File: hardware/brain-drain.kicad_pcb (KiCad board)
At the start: 4 copper layers, 180 x 110 mm, 311 parts, among them J10 SATA 22-pin, J11 SATA 22-pin, J12 SATA 22-pin, J13 SATA 22-pin, J21 KPJX-4S-S, J3 microSD, J4 RJ45 GbE magjack UDE RB1-125B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, J40 Fan GND/5V/TACH/PWM, J41 OLED GND/VCC/SCL/SDA, J5 USB-C rpiboot, J50 M.2 M-key, J6 nRPIBOOT, J7 UART0 GND/TX/RX, M1 CM5002016, Q1 2N7002, Q20 AO4407A, Q31 P-FET -30V 6A DFN3x3, Q32 P-FET -30V 6A DFN3x3, Q33 P-FET -30V 6A DFN3x3, Q34 P-FET -30V 6A DFN3x3, Q41 P-FET -30V 6A DFN3x3, Q42 P-FET -30V 6A DFN3x3, Q43 P-FET -30V 6A DFN3x3, Q44 P-FET -30V 6A DFN3x3, Q51 2N7002, Q52 2N7002, Q53 2N7002, Q54 2N7002, Q61 2N7002, Q62 2N7002, Q63 2N7002, Q64 2N7002, SW1 DIP x8, SW3 door microswitch, U1 USB5744/2G, U10 ASM1153E, U11 ASM1153E, U12 ASM1153E, U13 ASM1153E, U2 USB5744/2G, U20 TPS56637RPAR, U21 TPS56637RPAR, U22 AP63203WU-7, U3 AP2112K-1.2, U50 TPS22965DSGR, U51 AP63203WU-7, U52 TPS22965DSGR, Y1 25MHz CL=20pF, Y10 30MHz CL=16pF, Y11 30MHz CL=16pF, Y12 30MHz CL=16pF, Y13 30MHz CL=16pF, Y2 25MHz CL=20pF

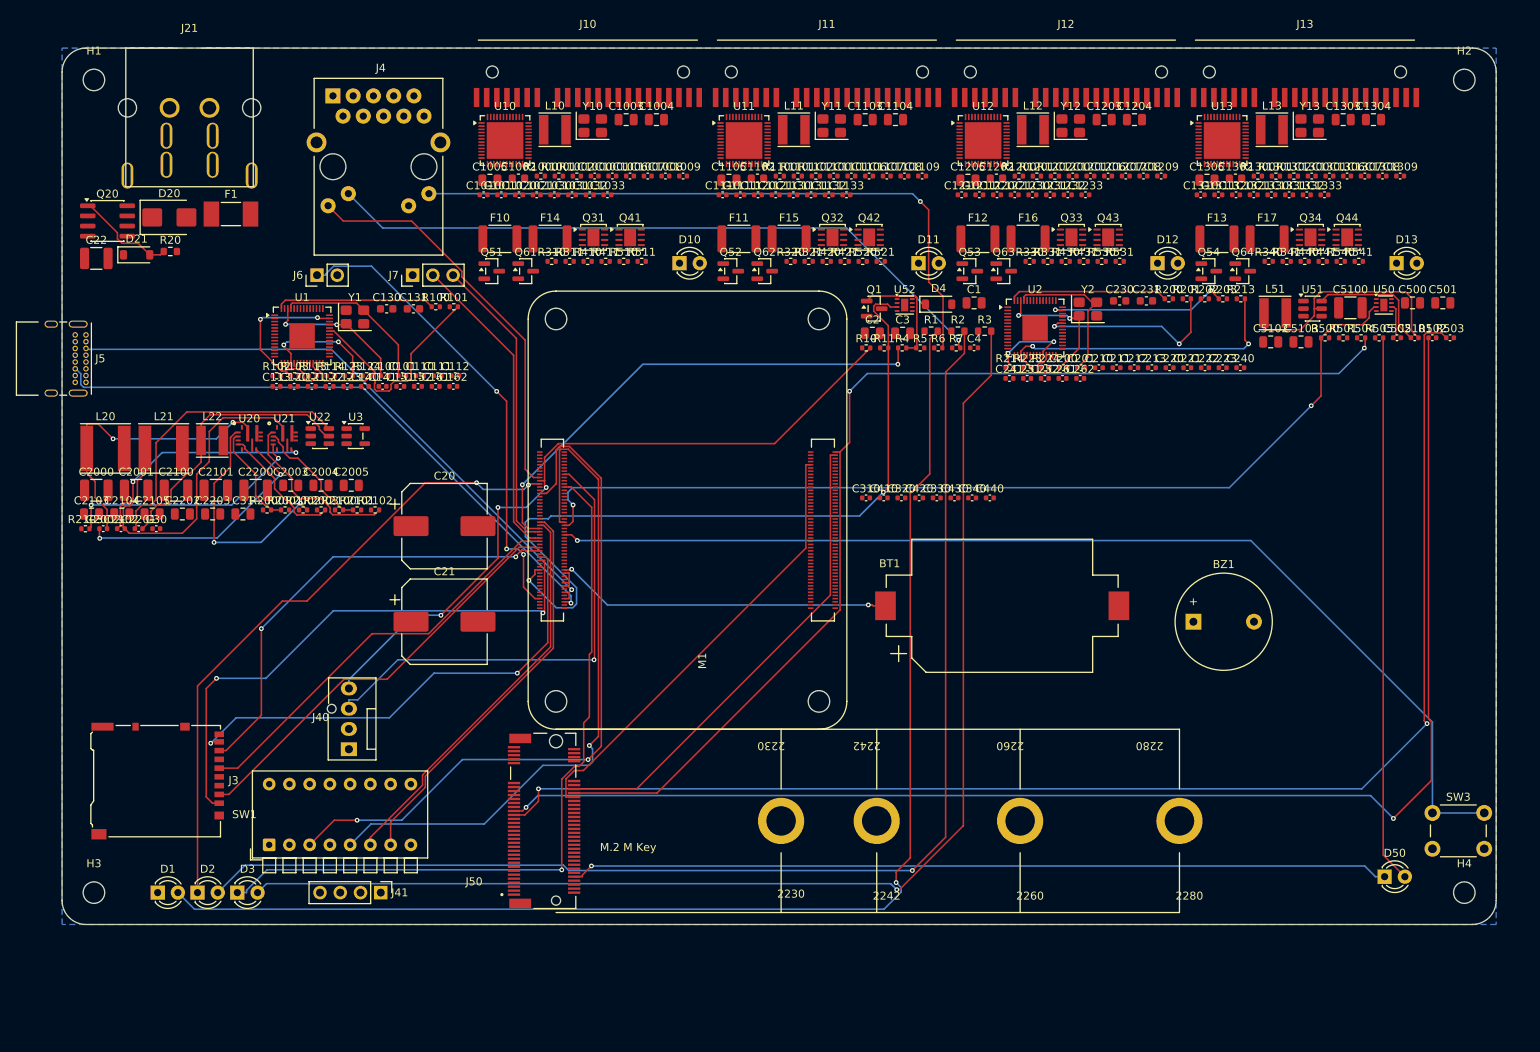
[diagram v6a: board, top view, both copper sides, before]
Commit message: design: portable brain box (C21) — board re-laid out at 150x98, cabled bays, enclosure v1, renders
- gen_pcb.py: new outline, walls (SATA rear; DIN/RJ45/USB-C left; microSD + M.2 slot front),
  CM5 landscape, M.2 vertical along the right edge, CR2032/buzzer on the bottom side
  (pcbnew flip post-process); check_place.py courtyard/outline checker; render_board.sh
- route.py: zones follow the new layout (polygon zones), origin/size from gen_pcb
- enclosure: closed box, drive rack removed, front-wall M.2 slot door, right-wall vents,
  buzzer floor holes, OLED window over the M.2 column; scene with four loose drives on cables;
  stl_preview camera fixed and triangles subdivided
- docs: C21 + D6 (option B parked), decision brief, STATUS R16-R18, panels for three walls,
  README/ARCHITECTURE/USAGE/BOM/CHANGELOG/HISTORY/tracker updated

Co-Authored-By: Claude Fable 5.1 <noreply@anthropic.com>
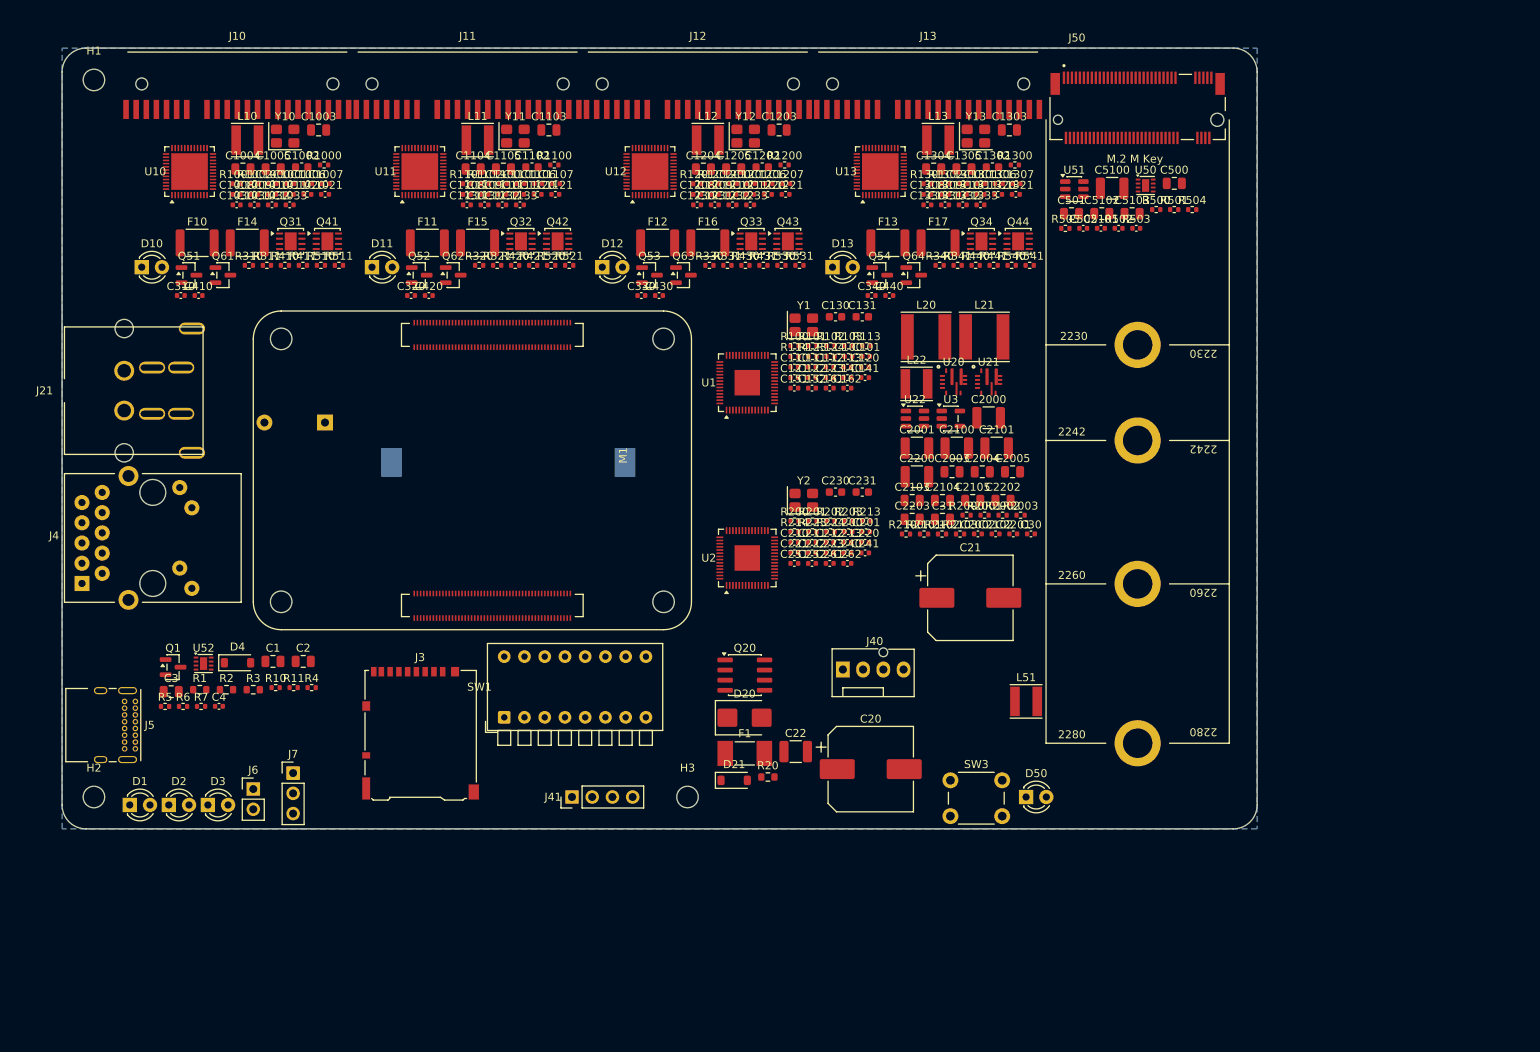
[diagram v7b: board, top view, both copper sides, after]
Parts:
- removed the C440 at (136.4, 76.5)
- BT1, BZ1: moved to B.Cu
- C1: renamed from R3; value 1k -> 22u 10V; footprint Resistor_SMD:R_0603_1608Metric -> Capacitor_SMD:C_0805_2012Metric
- C100: renamed from C112; value 100n -> 33p
- C1000: renamed from C1006; value 100n -> 22p
- C1001: renamed from C1007; value 100n -> 22p
- C1002: renamed from R1001; value 10k -> 2.2u; footprint Resistor_SMD:R_0402_1005Metric -> Capacitor_SMD:C_0603_1608Metric
- C1004: renamed from C1002; value 2.2u -> 10u 10V; footprint Capacitor_SMD:C_0603_1608Metric -> Capacitor_SMD:C_0805_2012Metric
- C1005: renamed from R1000; value 12.1k 1% -> 10u 10V; footprint Resistor_SMD:R_0402_1005Metric -> Capacitor_SMD:C_0805_2012Metric
- C101: renamed from C113; value 100n -> 33p
- C1020: renamed from C1030; value 10n -> 100n
- C1021: renamed from C1031; value 10n -> 100n
- C1032: renamed from F10; value 3A hold 1812 -> 10n; footprint Fuse:Fuse_1812_4532Metric -> Capacitor_SMD:C_0402_1005Metric
- C1033: renamed from F14; value 2A hold 1812 -> 10n; footprint Fuse:Fuse_1812_4532Metric -> Capacitor_SMD:C_0402_1005Metric
- C1101: renamed from C1106; value 100n -> 22p
- C1102: renamed from R1100; value 12.1k 1% -> 2.2u; footprint Resistor_SMD:R_0402_1005Metric -> Capacitor_SMD:C_0603_1608Metric
- C1105: renamed from C1102; value 2.2u -> 10u 10V; footprint Capacitor_SMD:C_0603_1608Metric -> Capacitor_SMD:C_0805_2012Metric
- C1121: renamed from C1130; value 10n -> 100n
- C1133: renamed from F11; value 3A hold 1812 -> 10n; footprint Fuse:Fuse_1812_4532Metric -> Capacitor_SMD:C_0402_1005Metric
- C130: renamed from R102; value 10k -> 4.7u 10V; footprint Resistor_SMD:R_0402_1005Metric -> Capacitor_SMD:C_0603_1608Metric
- C1300: renamed from R1302; value 470 -> 22p; footprint Resistor_SMD:R_0402_1005Metric -> Capacitor_SMD:C_0402_1005Metric
- C1302: renamed from C1305; value 10u 10V -> 2.2u; footprint Capacitor_SMD:C_0805_2012Metric -> Capacitor_SMD:C_0603_1608Metric
- C1303: renamed from Y13; value 30MHz CL=16pF -> 10u 10V; footprint Crystal:Crystal_SMD_3225-4Pin_3.2x2.5mm -> Capacitor_SMD:C_0805_2012Metric
- C1306: renamed from C1301; value 22p -> 100n
- C131: renamed from R103; value 200k -> 4.7u 10V; footprint Resistor_SMD:R_0402_1005Metric -> Capacitor_SMD:C_0603_1608Metric
- C1330: renamed from C1321; value 100n -> 10n
- C151: renamed from U2; value USB5744/2G -> 100n; footprint Package_DFN_QFN:QFN-56-1EP_7x7mm_P0.4mm_EP3.2x3.2mm -> Capacitor_SMD:C_0402_1005Metric
- C152: renamed from Y2; value 25MHz CL=20pF -> 100n; footprint Crystal:Crystal_SMD_3225-4Pin_3.2x2.5mm -> Capacitor_SMD:C_0402_1005Metric
- C161: renamed from C230; value 4.7u 10V -> 100n; footprint Capacitor_SMD:C_0603_1608Metric -> Capacitor_SMD:C_0402_1005Metric
- C162: renamed from C231; value 4.7u 10V -> 100n; footprint Capacitor_SMD:C_0603_1608Metric -> Capacitor_SMD:C_0402_1005Metric
- C2: renamed from R10; value 10k -> 22u 10V; footprint Resistor_SMD:R_0402_1005Metric -> Capacitor_SMD:C_0805_2012Metric
- C20: renamed from J21; value KPJX-4S-S -> 680u 25V low-ESR; footprint brain-drain:Kycon_KPJX-4S-S -> Capacitor_SMD:CP_Elec_10x10.5
- C200: renamed from C211; value 100n -> 33p
- C2000: renamed from C2004; value 22u 10V -> 10u 25V; footprint Capacitor_SMD:C_0805_2012Metric -> Capacitor_SMD:C_1210_3225Metric
- C2001: renamed from C2005; value 22u 10V -> 10u 25V; footprint Capacitor_SMD:C_0805_2012Metric -> Capacitor_SMD:C_1210_3225Metric
- C2002: renamed from C5100; value 10u 25V -> 100n 25V; footprint Capacitor_SMD:C_1210_3225Metric -> Capacitor_SMD:C_0402_1005Metric
- C2005: renamed from C31; value 10u 10V -> 22u 10V
- C201: renamed from C212; value 100n -> 33p
- C2100: renamed from C2103; value 22u 10V -> 10u 25V; footprint Capacitor_SMD:C_0805_2012Metric -> Capacitor_SMD:C_1210_3225Metric
- C2101: renamed from C2104; value 22u 10V -> 10u 25V; footprint Capacitor_SMD:C_0805_2012Metric -> Capacitor_SMD:C_1210_3225Metric
- C2102: renamed from U50; value TPS22965DSGR -> 100n 25V; footprint Package_SON:Texas_DSG0008A_WSON-8-1EP_2x2mm_P0.5mm_EP0.9x1.6mm -> Capacitor_SMD:C_0402_1005Metric
- C2103: renamed from R2000; value 73.2k -> 22u 10V; footprint Resistor_SMD:R_0402_1005Metric -> Capacitor_SMD:C_0805_2012Metric
- C2104: renamed from R2001; value 10k -> 22u 10V; footprint Resistor_SMD:R_0402_1005Metric -> Capacitor_SMD:C_0805_2012Metric
- C2105: renamed from R2002; value 100k -> 22u 10V; footprint Resistor_SMD:R_0402_1005Metric -> Capacitor_SMD:C_0805_2012Metric
- C22: renamed from U20; value TPS56637RPAR -> 10u 25V; footprint brain-drain:Texas_RPA0010A_VQFN-HR-10_3x3mm -> Capacitor_SMD:C_1210_3225Metric
- C2200: renamed from C2105; value 22u 10V -> 10u 25V; footprint Capacitor_SMD:C_0805_2012Metric -> Capacitor_SMD:C_1210_3225Metric
- C2201: renamed from C500; value 10u 10V -> 100n 10V; footprint Capacitor_SMD:C_0805_2012Metric -> Capacitor_SMD:C_0402_1005Metric
- C2202: renamed from R2003; value 10k -> 22u 10V; footprint Resistor_SMD:R_0402_1005Metric -> Capacitor_SMD:C_0805_2012Metric
- C2203: renamed from R2100; value 73.2k -> 22u 10V; footprint Resistor_SMD:R_0402_1005Metric -> Capacitor_SMD:C_0805_2012Metric
- C230: renamed from R201; value 10k -> 4.7u 10V; footprint Resistor_SMD:R_0402_1005Metric -> Capacitor_SMD:C_0603_1608Metric
- C231: renamed from R202; value 10k -> 4.7u 10V; footprint Resistor_SMD:R_0402_1005Metric -> Capacitor_SMD:C_0603_1608Metric
- C252: renamed from U10; value ASM1153E -> 100n; footprint Package_DFN_QFN:QFN-48-1EP_6x6mm_P0.4mm_EP4.6x4.6mm -> Capacitor_SMD:C_0402_1005Metric
- C261: renamed from L10; value 4.7u 1A -> 100n; footprint Inductor_SMD:L_Taiyo-Yuden_NR-40xx -> Capacitor_SMD:C_0402_1005Metric
- C262: renamed from Y10; value 30MHz CL=16pF -> 100n; footprint Crystal:Crystal_SMD_3225-4Pin_3.2x2.5mm -> Capacitor_SMD:C_0402_1005Metric
- C3: renamed from R11; value 10k -> 10u 10V; footprint Resistor_SMD:R_0402_1005Metric -> Capacitor_SMD:C_0805_2012Metric
- C30: renamed from C501; value 22u 10V -> 1u 10V; footprint Capacitor_SMD:C_0805_2012Metric -> Capacitor_SMD:C_0402_1005Metric
- C31: renamed from R2101; value 10k -> 10u 10V; footprint Resistor_SMD:R_0402_1005Metric -> Capacitor_SMD:C_0805_2012Metric
- C310: renamed from U11; value ASM1153E -> 100n; footprint Package_DFN_QFN:QFN-48-1EP_6x6mm_P0.4mm_EP4.6x4.6mm -> Capacitor_SMD:C_0402_1005Metric
- C340: renamed from R541; value 1k -> 100n; footprint Resistor_SMD:R_0402_1005Metric -> Capacitor_SMD:C_0402_1005Metric
- C4: renamed from R100; value 12.0k 1% -> 1u 10V; footprint Resistor_SMD:R_0402_1005Metric -> Capacitor_SMD:C_0402_1005Metric
- C410: renamed from L11; value 4.7u 1A -> 100n; footprint Inductor_SMD:L_Taiyo-Yuden_NR-40xx -> Capacitor_SMD:C_0402_1005Metric
- C420: renamed from U12; value ASM1153E -> 100n; footprint Package_DFN_QFN:QFN-48-1EP_6x6mm_P0.4mm_EP4.6x4.6mm -> Capacitor_SMD:C_0402_1005Metric
- C500: renamed from R501; value 10k -> 10u 10V; footprint Resistor_SMD:R_0402_1005Metric -> Capacitor_SMD:C_0805_2012Metric
- C501: renamed from R504; value 10k -> 22u 10V; footprint Resistor_SMD:R_0402_1005Metric -> Capacitor_SMD:C_0805_2012Metric
- C502: renamed from U52; value TPS22965DSGR -> 1n; footprint Package_SON:Texas_DSG0008A_WSON-8-1EP_2x2mm_P0.5mm_EP0.9x1.6mm -> Capacitor_SMD:C_0402_1005Metric
- C5100: renamed from C5103; value 22u 10V -> 10u 25V; footprint Capacitor_SMD:C_0805_2012Metric -> Capacitor_SMD:C_1210_3225Metric
- C5101: renamed from D4; value 1N4148W -> 100n 10V; footprint Diode_SMD:D_SOD-123 -> Capacitor_SMD:C_0402_1005Metric
- C5102: renamed from R505; value 470 -> 22u 10V; footprint Resistor_SMD:R_0402_1005Metric -> Capacitor_SMD:C_0805_2012Metric
- C5103: renamed from C502; value 1n -> 22u 10V; footprint Capacitor_SMD:C_0402_1005Metric -> Capacitor_SMD:C_0805_2012Metric
- D10: renamed from J12; value SATA 22-pin -> blue bay activity; footprint brain-drain:SATA_22pin_Receptacle_RA -> LED_THT:LED_D3.0mm
- D12: renamed from SW3; value door microswitch -> blue bay activity; footprint Button_Switch_THT:SW_PUSH_6mm -> LED_THT:LED_D3.0mm
- D13: renamed from F1; value 10A slow 0453010.MR -> blue bay activity; footprint Fuse:Fuse_Littelfuse-NANO2-451_453 -> LED_THT:LED_D3.0mm
- D20: renamed from L21; value 2.2u 8A -> SMBJ15A; footprint Inductor_SMD:L_Taiyo-Yuden_NR-60xx -> Diode_SMD:D_SMB
- D21: renamed from U21; value TPS56637RPAR -> 12V 0.5W; footprint brain-drain:Texas_RPA0010A_VQFN-HR-10_3x3mm -> Diode_SMD:D_SOD-123
- D4: renamed from R2; value 1k -> 1N4148W; footprint Resistor_SMD:R_0603_1608Metric -> Diode_SMD:D_SOD-123
- D50: renamed from D21; value 12V 0.5W -> blue M.2 activity; footprint Diode_SMD:D_SOD-123 -> LED_THT:LED_D3.0mm
- F1: renamed from L22; value 4.7u 3A -> 10A slow 0453010.MR; footprint Inductor_SMD:L_Taiyo-Yuden_NR-40xx -> Fuse:Fuse_Littelfuse-NANO2-451_453
- F10: renamed from Q31; value P-FET -30V 6A DFN3x3 -> 3A hold 1812; footprint Package_DFN_QFN:DFN-8-1EP_3x3mm_P0.65mm_EP1.5x2.25mm -> Fuse:Fuse_1812_4532Metric
- F11: renamed from F15; value 2A hold 1812 -> 3A hold 1812
- F13: renamed from C1333; value 10n -> 3A hold 1812; footprint Capacitor_SMD:C_0402_1005Metric -> Fuse:Fuse_1812_4532Metric
- F14: renamed from Q41; value P-FET -30V 6A DFN3x3 -> 2A hold 1812; footprint Package_DFN_QFN:DFN-8-1EP_3x3mm_P0.65mm_EP1.5x2.25mm -> Fuse:Fuse_1812_4532Metric
- F15: renamed from Q32; value P-FET -30V 6A DFN3x3 -> 2A hold 1812; footprint Package_DFN_QFN:DFN-8-1EP_3x3mm_P0.65mm_EP1.5x2.25mm -> Fuse:Fuse_1812_4532Metric
- F17: renamed from F13; value 3A hold 1812 -> 2A hold 1812
- J10: renamed from D11; value blue bay activity -> SATA 22-pin; footprint LED_THT:LED_D3.0mm -> brain-drain:SATA_22pin_Receptacle_RA
- J12: renamed from D50; value blue M.2 activity -> SATA 22-pin; footprint LED_THT:LED_D3.0mm -> brain-drain:SATA_22pin_Receptacle_RA
- J13: renamed from D20; value SMBJ15A -> SATA 22-pin; footprint Diode_SMD:D_SMB -> brain-drain:SATA_22pin_Receptacle_RA
- J21: renamed from H4; value M2.5 -> KPJX-4S-S; footprint MountingHole:MountingHole_2.7mm_M2.5 -> brain-drain:Kycon_KPJX-4S-S
- J50: renamed from C22; value 10u 25V -> M.2 M-key; footprint Capacitor_SMD:C_1210_3225Metric -> brain-drain:M2_Socket3_MKey_CM5IO
- L10: renamed from C1003; value 10u 10V -> 4.7u 1A; footprint Capacitor_SMD:C_0805_2012Metric -> Inductor_SMD:L_Taiyo-Yuden_NR-40xx
- L11: renamed from Y11; value 30MHz CL=16pF -> 4.7u 1A; footprint Crystal:Crystal_SMD_3225-4Pin_3.2x2.5mm -> Inductor_SMD:L_Taiyo-Yuden_NR-40xx
- L13: renamed from U13; value ASM1153E -> 4.7u 1A; footprint Package_DFN_QFN:QFN-48-1EP_6x6mm_P0.4mm_EP4.6x4.6mm -> Inductor_SMD:L_Taiyo-Yuden_NR-40xx
- L20: renamed from U3; value AP2112K-1.2 -> 2.2u 8A; footprint Package_TO_SOT_SMD:SOT-23-5 -> Inductor_SMD:L_Taiyo-Yuden_NR-60xx
- L21: renamed from C2000; value 10u 25V -> 2.2u 8A; footprint Capacitor_SMD:C_1210_3225Metric -> Inductor_SMD:L_Taiyo-Yuden_NR-60xx
- L22: renamed from C2001; value 10u 25V -> 4.7u 3A; footprint Capacitor_SMD:C_1210_3225Metric -> Inductor_SMD:L_Taiyo-Yuden_NR-40xx
- L51: renamed from C21; value 680u 25V low-ESR -> 4.7u 3A; footprint Capacitor_SMD:CP_Elec_10x10.5 -> Inductor_SMD:L_Taiyo-Yuden_NR-40xx
- Q1: renamed from C3; value 10u 10V -> 2N7002; footprint Capacitor_SMD:C_0805_2012Metric -> Package_TO_SOT_SMD:SOT-23
- Q20: renamed from L20; value 2.2u 8A -> AO4407A; footprint Inductor_SMD:L_Taiyo-Yuden_NR-60xx -> Package_SO:SOIC-8_3.9x4.9mm_P1.27mm
- Q31: renamed from Q51; value 2N7002 -> P-FET -30V 6A DFN3x3; footprint Package_TO_SOT_SMD:SOT-23 -> Package_DFN_QFN:DFN-8-1EP_3x3mm_P0.65mm_EP1.5x2.25mm
- Q34: renamed from F17; value 2A hold 1812 -> P-FET -30V 6A DFN3x3; footprint Fuse:Fuse_1812_4532Metric -> Package_DFN_QFN:DFN-8-1EP_3x3mm_P0.65mm_EP1.5x2.25mm
- Q41: renamed from Q61; value 2N7002 -> P-FET -30V 6A DFN3x3; footprint Package_TO_SOT_SMD:SOT-23 -> Package_DFN_QFN:DFN-8-1EP_3x3mm_P0.65mm_EP1.5x2.25mm
- Q42: renamed from Q52; value 2N7002 -> P-FET -30V 6A DFN3x3; footprint Package_TO_SOT_SMD:SOT-23 -> Package_DFN_QFN:DFN-8-1EP_3x3mm_P0.65mm_EP1.5x2.25mm
- Q51: renamed from R310; value 100k -> 2N7002; footprint Resistor_SMD:R_0402_1005Metric -> Package_TO_SOT_SMD:SOT-23
- Q54: renamed from Q44; value P-FET -30V 6A DFN3x3 -> 2N7002; footprint Package_DFN_QFN:DFN-8-1EP_3x3mm_P0.65mm_EP1.5x2.25mm -> Package_TO_SOT_SMD:SOT-23
- Q61: renamed from R311; value 10k -> 2N7002; footprint Resistor_SMD:R_0402_1005Metric -> Package_TO_SOT_SMD:SOT-23
- Q62: renamed from R320; value 100k -> 2N7002; footprint Resistor_SMD:R_0402_1005Metric -> Package_TO_SOT_SMD:SOT-23
- R1: renamed from R4; footprint Resistor_SMD:R_0402_1005Metric -> Resistor_SMD:R_0603_1608Metric
- R10: renamed from R7; value 470 -> 10k
- R100: renamed from R113; value 10k -> 12.0k 1%
- R1000: renamed from R1002; value 470 -> 12.1k 1%
- R1001: renamed from C1000; value 22p -> 10k; footprint Capacitor_SMD:C_0402_1005Metric -> Resistor_SMD:R_0402_1005Metric
- R1002: renamed from C1001; value 22p -> 470; footprint Capacitor_SMD:C_0402_1005Metric -> Resistor_SMD:R_0402_1005Metric
- R103: renamed from R124; value 10k -> 200k
- R11: renamed from C4; value 1u 10V -> 10k; footprint Capacitor_SMD:C_0402_1005Metric -> Resistor_SMD:R_0402_1005Metric
- R1100: renamed from R1101; value 10k -> 12.1k 1%
- R1101: renamed from R1102; value 470 -> 10k
- R1102: renamed from C1100; value 22p -> 470; footprint Capacitor_SMD:C_0402_1005Metric -> Resistor_SMD:R_0402_1005Metric
- R113: renamed from C100; value 33p -> 10k; footprint Capacitor_SMD:C_0402_1005Metric -> Resistor_SMD:R_0402_1005Metric
- R114: renamed from C101; value 33p -> 10k; footprint Capacitor_SMD:C_0402_1005Metric -> Resistor_SMD:R_0402_1005Metric
- R123: renamed from C110; value 100n -> 10k; footprint Capacitor_SMD:C_0402_1005Metric -> Resistor_SMD:R_0402_1005Metric
- R124: renamed from C111; value 100n -> 10k; footprint Capacitor_SMD:C_0402_1005Metric -> Resistor_SMD:R_0402_1005Metric
- R1300: renamed from C1302; value 2.2u -> 12.1k 1%; footprint Capacitor_SMD:C_0603_1608Metric -> Resistor_SMD:R_0402_1005Metric
- R1301: renamed from R1300; value 12.1k 1% -> 10k
- R1302: renamed from R1301; value 10k -> 470
- R2: renamed from R5; value 100k -> 1k; footprint Resistor_SMD:R_0402_1005Metric -> Resistor_SMD:R_0603_1608Metric
- R20: renamed from U22; value AP63203WU-7 -> 100k; footprint Package_TO_SOT_SMD:TSOT-23-6 -> Resistor_SMD:R_0603_1608Metric
- R200: renamed from R203; value 200k -> 12.0k 1%
- R2000: renamed from R2102; value 100k -> 73.2k
- R2002: renamed from C2002; value 100n 25V -> 100k; footprint Capacitor_SMD:C_0402_1005Metric -> Resistor_SMD:R_0402_1005Metric
- R2003: renamed from C2102; value 100n 25V -> 10k; footprint Capacitor_SMD:C_0402_1005Metric -> Resistor_SMD:R_0402_1005Metric
- R203: renamed from R223; value 10k -> 200k
- R2100: renamed from C2201; value 100n 10V -> 73.2k; footprint Capacitor_SMD:C_0402_1005Metric -> Resistor_SMD:R_0402_1005Metric
- R2101: renamed from C30; value 1u 10V -> 10k; footprint Capacitor_SMD:C_0402_1005Metric -> Resistor_SMD:R_0402_1005Metric
- R2102: renamed from L51; value 4.7u 3A -> 100k; footprint Inductor_SMD:L_Taiyo-Yuden_NR-40xx -> Resistor_SMD:R_0402_1005Metric
- R2103: renamed from U51; value AP63203WU-7 -> 10k; footprint Package_TO_SOT_SMD:TSOT-23-6 -> Resistor_SMD:R_0402_1005Metric
- R214: renamed from C200; value 33p -> 10k; footprint Capacitor_SMD:C_0402_1005Metric -> Resistor_SMD:R_0402_1005Metric
- R223: renamed from C201; value 33p -> 10k; footprint Capacitor_SMD:C_0402_1005Metric -> Resistor_SMD:R_0402_1005Metric
- R224: renamed from C210; value 100n -> 10k; footprint Capacitor_SMD:C_0402_1005Metric -> Resistor_SMD:R_0402_1005Metric
- R3: renamed from R6; value 470 -> 1k; footprint Resistor_SMD:R_0402_1005Metric -> Resistor_SMD:R_0603_1608Metric
- R320: renamed from R321; value 10k -> 100k
- R321: renamed from R420; value 100k -> 10k
- R340: renamed from Q64; value 2N7002 -> 100k; footprint Package_TO_SOT_SMD:SOT-23 -> Resistor_SMD:R_0402_1005Metric
- R341: renamed from R340; value 100k -> 10k
- R4: renamed from U1; value USB5744/2G -> 1k; footprint Package_DFN_QFN:QFN-56-1EP_7x7mm_P0.4mm_EP3.2x3.2mm -> Resistor_SMD:R_0402_1005Metric
- R410: renamed from R510; value 10k -> 100k
- R411: renamed from R511; value 1k -> 10k
- R420: renamed from R421; value 10k -> 100k
- R440: renamed from R341; value 10k -> 100k
- R441: renamed from R440; value 100k -> 10k
- R5: renamed from Y1; value 25MHz CL=20pF -> 100k; footprint Crystal:Crystal_SMD_3225-4Pin_3.2x2.5mm -> Resistor_SMD:R_0402_1005Metric
- R500: renamed from C5101; value 100n 10V -> 10k; footprint Capacitor_SMD:C_0402_1005Metric -> Resistor_SMD:R_0402_1005Metric
- R501: renamed from R502; value 0R (cap DNP alt) -> 10k; footprint Capacitor_SMD:C_0402_1005Metric -> Resistor_SMD:R_0402_1005Metric
- R502: renamed from C1; value 22u 10V -> 0R (cap DNP alt); footprint Capacitor_SMD:C_0805_2012Metric -> Capacitor_SMD:C_0402_1005Metric
- R503: renamed from C2; value 22u 10V -> 0R (cap DNP alt); footprint Capacitor_SMD:C_0805_2012Metric -> Capacitor_SMD:C_0402_1005Metric
- R504: renamed from R503; value 0R (cap DNP alt) -> 10k; footprint Capacitor_SMD:C_0402_1005Metric -> Resistor_SMD:R_0402_1005Metric
- R505: renamed from Q1; value 2N7002 -> 470; footprint Package_TO_SOT_SMD:SOT-23 -> Resistor_SMD:R_0402_1005Metric
- R510: renamed from C310; value 100n -> 10k; footprint Capacitor_SMD:C_0402_1005Metric -> Resistor_SMD:R_0402_1005Metric
- R511: renamed from C410; value 100n -> 1k; footprint Capacitor_SMD:C_0402_1005Metric -> Resistor_SMD:R_0402_1005Metric
- R520: renamed from R521; value 1k -> 10k
- R521: renamed from C320; value 100n -> 1k; footprint Capacitor_SMD:C_0402_1005Metric -> Resistor_SMD:R_0402_1005Metric
- R541: renamed from R540; value 10k -> 1k
- R6: renamed from C130; value 4.7u 10V -> 470; footprint Capacitor_SMD:C_0603_1608Metric -> Resistor_SMD:R_0402_1005Metric
- R7: renamed from C131; value 4.7u 10V -> 470; footprint Capacitor_SMD:C_0603_1608Metric -> Resistor_SMD:R_0402_1005Metric
- SW3: renamed from R20; value 100k -> door microswitch; footprint Resistor_SMD:R_0603_1608Metric -> Button_Switch_THT:SW_PUSH_6mm
- U1: renamed from J10; value SATA 22-pin -> USB5744/2G; footprint brain-drain:SATA_22pin_Receptacle_RA -> Package_DFN_QFN:QFN-56-1EP_7x7mm_P0.4mm_EP3.2x3.2mm
- U10: renamed from J11; value SATA 22-pin -> ASM1153E; footprint brain-drain:SATA_22pin_Receptacle_RA -> Package_DFN_QFN:QFN-48-1EP_6x6mm_P0.4mm_EP4.6x4.6mm
- U11: renamed from D12; value blue bay activity -> ASM1153E; footprint LED_THT:LED_D3.0mm -> Package_DFN_QFN:QFN-48-1EP_6x6mm_P0.4mm_EP4.6x4.6mm
- U12: renamed from J50; value M.2 M-key -> ASM1153E; footprint brain-drain:M2_Socket3_MKey_CM5IO -> Package_DFN_QFN:QFN-48-1EP_6x6mm_P0.4mm_EP4.6x4.6mm
- U13: renamed from Q20; value AO4407A -> ASM1153E; footprint Package_SO:SOIC-8_3.9x4.9mm_P1.27mm -> Package_DFN_QFN:QFN-48-1EP_6x6mm_P0.4mm_EP4.6x4.6mm
- U2: renamed from D10; value blue bay activity -> USB5744/2G; footprint LED_THT:LED_D3.0mm -> Package_DFN_QFN:QFN-56-1EP_7x7mm_P0.4mm_EP3.2x3.2mm
- U20: renamed from C2100; value 10u 25V -> TPS56637RPAR; footprint Capacitor_SMD:C_1210_3225Metric -> brain-drain:Texas_RPA0010A_VQFN-HR-10_3x3mm
- U21: renamed from C2101; value 10u 25V -> TPS56637RPAR; footprint Capacitor_SMD:C_1210_3225Metric -> brain-drain:Texas_RPA0010A_VQFN-HR-10_3x3mm
- U22: renamed from C2200; value 10u 25V -> AP63203WU-7; footprint Capacitor_SMD:C_1210_3225Metric -> Package_TO_SOT_SMD:TSOT-23-6
- U3: renamed from C2003; value 22u 10V -> AP2112K-1.2; footprint Capacitor_SMD:C_0805_2012Metric -> Package_TO_SOT_SMD:SOT-23-5
- U50: renamed from R500; value 10k -> TPS22965DSGR; footprint Resistor_SMD:R_0402_1005Metric -> Package_SON:Texas_DSG0008A_WSON-8-1EP_2x2mm_P0.5mm_EP0.9x1.6mm
- U51: renamed from C5102; value 22u 10V -> AP63203WU-7; footprint Capacitor_SMD:C_0805_2012Metric -> Package_TO_SOT_SMD:TSOT-23-6
- U52: renamed from R1; value 1k -> TPS22965DSGR; footprint Resistor_SMD:R_0603_1608Metric -> Package_SON:Texas_DSG0008A_WSON-8-1EP_2x2mm_P0.5mm_EP0.9x1.6mm
- Y1: renamed from R101; value 10k -> 25MHz CL=20pF; footprint Resistor_SMD:R_0402_1005Metric -> Crystal:Crystal_SMD_3225-4Pin_3.2x2.5mm
- Y10: renamed from C1004; value 10u 10V -> 30MHz CL=16pF; footprint Capacitor_SMD:C_0805_2012Metric -> Crystal:Crystal_SMD_3225-4Pin_3.2x2.5mm
- Y11: renamed from C1103; value 10u 10V -> 30MHz CL=16pF; footprint Capacitor_SMD:C_0805_2012Metric -> Crystal:Crystal_SMD_3225-4Pin_3.2x2.5mm
- Y13: renamed from L13; value 4.7u 1A -> 30MHz CL=16pF; footprint Inductor_SMD:L_Taiyo-Yuden_NR-40xx -> Crystal:Crystal_SMD_3225-4Pin_3.2x2.5mm
- Y2: renamed from R200; value 12.0k 1% -> 25MHz CL=20pF; footprint Resistor_SMD:R_0402_1005Metric -> Crystal:Crystal_SMD_3225-4Pin_3.2x2.5mm
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- renumbered C1005 to C1003, C1008 to C1006, C1009 to C1007, C1010 to C1008, C1011 to C1009, C1020 to C1010, C1021 to C1011, C1032 to C1030, C1033 to C1031, C120 to C110, C1101 to C1100, C1104 to C1103, C1105 to C1104, C1107 to C1106, C1108 to C1107, C1109 to C1108, C1110 to C1109, C121 to C111, C1111 to C1110, C1120 to C1111, C122 to C112, C1121 to C1120, C123 to C113, C1131 to C1130, C1132 to C1131, C1133 to C1132, C140 to C120, C141 to C121, C151 to C122, C152 to C123, C1300 to C1301, C1303 to C1304, C1304 to C1305, C1306 to C1307, C1307 to C1308, C1308 to C1309, C1309 to C1310, C1310 to C1311, C1311 to C1320, C1320 to C1321, C1330 to C1331, C1331 to C1332, C1332 to C1333, C161 to C140, C162 to C141, C2202 to C2003, C2203 to C2004, C20 to C21, C213 to C210, C220 to C211, C221 to C212, C222 to C213, C223 to C220, C240 to C221, C241 to C222, C251 to C223, C252 to C240, C261 to C241, C262 to C251, C420 to C320, C340 to C440, D13 to D11, J13 to J11, Q42 to Q32, Q34 to Q44, Q62 to Q52, Q54 to Q64, R114 to R101, R123 to R102, R2103 to R2001, R213 to R201, R214 to R202, R224 to R213, R410 to R310, R411 to R311, R520 to R421, R441 to R540
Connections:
- C1 pad 1: +3V3 -> 5V_SYS
- C1 pad 2: D3_A -> GND
- C100 pad 1: +3V3 -> U1_XTALI
- C1000 pad 1: U10_VDD_CORE -> U10_XI
- C1001 pad 1: U10_VDD_CORE -> U10_XO
- C1002 pad 1: U10_VCCO -> U10_RST
- C1002 pad 2: U10_RST -> GND
- C1003 pad 1: U10_VCCO -> U10_VDD_CORE
- C1004 pad 1: U10_RST -> 5V_SYS
- C1005 pad 1: U10_REXT -> U10_VCCO
- C1006 pad 1: U10_VCCO -> U10_VDD_CORE
- C1007 pad 1: U10_VCCO -> U10_VDD_CORE
- C101 pad 1: +3V3 -> U1_XTALO
- C1010 pad 1: U10_UTXP -> U10_VCCO
- C1010 pad 2: BAY1_USB3_TX_P -> GND
- C1011 pad 1: U10_UTXN -> U10_VCCO
- C1011 pad 2: BAY1_USB3_TX_N -> GND
- C1020 pad 1: U10_STXP -> U10_UTXP
- C1020 pad 2: BAY1_SATA_A_P -> BAY1_USB3_TX_P
- C1021 pad 1: U10_STXN -> U10_UTXN
- C1021 pad 2: BAY1_SATA_A_N -> BAY1_USB3_TX_N
- C1030 pad 1: BAY1_SATA_B_P -> U10_STXP
- C1030 pad 2: U10_SRXP -> BAY1_SATA_A_P
- C1031 pad 1: BAY1_SATA_B_N -> U10_STXN
- C1031 pad 2: U10_SRXN -> BAY1_SATA_A_N
- C1032 pad 1: 12V_BAY1_SW -> BAY1_SATA_B_P
- C1032 pad 2: 12V_BAY1 -> U10_SRXP
- C1033 pad 1: 5V_BAY1_SW -> BAY1_SATA_B_N
- C1033 pad 2: 5V_BAY1 -> U10_SRXN
- C110 pad 1: +1V2 -> +3V3
- C1100 pad 1: U11_XO -> U11_XI
- C1101 pad 1: U11_VDD_CORE -> U11_XO
- C1102 pad 1: U11_REXT -> U11_RST
- C1103 pad 1: 5V_SYS -> U11_VDD_CORE
- C1104 pad 1: U11_VCCO -> 5V_SYS
- C1105 pad 1: U11_RST -> U11_VCCO
- C1107 pad 1: U11_VCCO -> U11_VDD_CORE
- C111 pad 1: +1V2 -> +3V3
- C1111 pad 1: U11_UTXP -> U11_VCCO
- C1111 pad 2: BAY2_USB3_TX_P -> GND
- C112 pad 1: +1V2 -> +3V3
- C1120 pad 1: U11_UTXN -> U11_UTXP
- C1120 pad 2: BAY2_USB3_TX_N -> BAY2_USB3_TX_P
- C1121 pad 1: U11_STXP -> U11_UTXN
- C1121 pad 2: BAY2_SATA_A_P -> BAY2_USB3_TX_N
- C113 pad 1: +1V2 -> +3V3
- C1130 pad 1: U11_STXN -> U11_STXP
- C1130 pad 2: BAY2_SATA_A_N -> BAY2_SATA_A_P
- C1131 pad 1: BAY2_SATA_B_P -> U11_STXN
- C1131 pad 2: U11_SRXP -> BAY2_SATA_A_N
- C1132 pad 1: BAY2_SATA_B_N -> BAY2_SATA_B_P
- C1132 pad 2: U11_SRXN -> U11_SRXP
- C1133 pad 1: 12V_BAY2_SW -> BAY2_SATA_B_N
- C1133 pad 2: 12V_BAY2 -> U11_SRXN
- C120 pad 1: U1_UP_TXDP -> +1V2
- C120 pad 2: USB3_0_RX_P -> GND
- C121 pad 1: U1_UP_TXDM -> +1V2
- C121 pad 2: USB3_0_RX_N -> GND
- C122 pad 1: U1_DN1_TXDP -> +1V2
- C122 pad 2: BAY1_USB3_RX_P -> GND
- C123 pad 1: U1_DN2_TXDP -> +1V2
- C123 pad 2: BAY2_USB3_RX_P -> GND
- C130 pad 2: U1_RESET_N -> GND
- C1300 pad 1: U13_VCCO -> U13_XI
- C1300 pad 2: BAY4_LED_A -> GND
- C1301 pad 1: U13_XI -> U13_XO
- C1302 pad 1: U13_VCCO -> U13_RST
- C1303 pad 1: U13_XI -> U13_VDD_CORE
- C1304 pad 1: U13_VDD_CORE -> 5V_SYS
- C1305 pad 1: 5V_SYS -> U13_VCCO
- C1306 pad 1: U13_XO -> U13_VDD_CORE
- C1308 pad 1: U13_VDD_CORE -> U13_VCCO
- C131 pad 1: U1_CFG_NON_REM -> +1V2
- C1320 pad 1: U13_VCCO -> U13_UTXP
- C1320 pad 2: GND -> BAY4_USB3_TX_P
- C1321 pad 1: U13_UTXP -> U13_UTXN
- C1321 pad 2: BAY4_USB3_TX_P -> BAY4_USB3_TX_N
- C1330 pad 1: U13_UTXN -> U13_STXP
- C1330 pad 2: BAY4_USB3_TX_N -> BAY4_SATA_A_P
- C1331 pad 1: U13_STXP -> U13_STXN
- C1331 pad 2: BAY4_SATA_A_P -> BAY4_SATA_A_N
- C1332 pad 1: U13_STXN -> BAY4_SATA_B_P
- C1332 pad 2: BAY4_SATA_A_N -> U13_SRXP
- C1333 pad 1: BAY4_SATA_B_P -> BAY4_SATA_B_N
- C1333 pad 2: U13_SRXP -> U13_SRXN
- C140 pad 1: U1_DN1_TXDM -> U1_UP_TXDP
- C140 pad 2: BAY1_USB3_RX_N -> USB3_0_RX_P
- C141 pad 1: U1_DN2_TXDM -> U1_UP_TXDM
- C141 pad 2: BAY2_USB3_RX_N -> USB3_0_RX_N
- C151 pad 1: BAY3_USB2_DP -> U1_DN1_TXDP
- C151 pad 2: BAY3_USB2_DM -> BAY1_USB3_RX_P
- C152 pad 1: U2_XTALI -> U1_DN2_TXDP
- C152 pad 2: GND -> BAY2_USB3_RX_P
- C161 pad 1: +3V3 -> U1_DN1_TXDM
- C161 pad 2: GND -> BAY1_USB3_RX_N
- C162 pad 1: +1V2 -> U1_DN2_TXDM
- C162 pad 2: GND -> BAY2_USB3_RX_N
- C2 pad 1: +3V3 -> 5V_SYS
- C2 pad 2: FAN_PWM -> GND
- C20 pad 1: VIN_12V_RAW -> +12V
- C20 pad 2: VIN_12V_RAW -> GND
- C200 pad 1: +3V3 -> U2_XTALI
- C2000 pad 1: 5V_SYS -> +12V
- C2001 pad 1: 5V_SYS -> +12V
- C2002 pad 1: +12V -> U20_BOOT
- C2002 pad 2: GND -> U20_SW
- C2003 pad 1: +3V3 -> 5V_SYS
- C2004 pad 1: +3V3 -> 5V_SYS
- C2005 pad 1: +1V2 -> 5V_SYS
- C201 pad 1: +3V3 -> U2_XTALO
- C2100 pad 1: 5V_HDD -> +12V
- C2101 pad 1: 5V_HDD -> +12V
- C2102 pad 1: 3V3_M2 -> U21_BOOT
- C2102 pad 2: 3V3_M2 -> U21_SW
- C2103 pad 1: 5V_SYS -> 5V_HDD
- C2103 pad 2: U20_FB -> GND
- C2104 pad 1: U20_FB -> 5V_HDD
- C2105 pad 1: +12V -> 5V_HDD
- C2105 pad 2: U20_EN -> GND
- C211 pad 1: +1V2 -> +3V3
- C212 pad 1: +1V2 -> +3V3
- C213 pad 1: +1V2 -> +3V3
- C22 pad 1: U20_EN -> +12V
- C22 pad 2: U20_FB -> GND
- C2200 pad 1: 5V_HDD -> +12V
- C2201 pad 1: 3V3_M2 -> U22_BST
- C2201 pad 2: GND -> U22_SW
- C2202 pad 1: 5V_SYS -> +3V3
- C2202 pad 2: PG_5V_SYS -> GND
- C2203 pad 1: 5V_HDD -> +3V3
- C2203 pad 2: U21_FB -> GND
- C221 pad 1: U2_UP_TXDP -> +1V2
- C221 pad 2: USB3_1_RX_P -> GND
- C222 pad 1: U2_UP_TXDM -> +1V2
- C222 pad 2: USB3_1_RX_N -> GND
- C223 pad 1: U2_DN1_TXDP -> +1V2
- C223 pad 2: BAY3_USB3_RX_P -> GND
- C230 pad 2: U2_VBUS_DET -> GND
- C231 pad 1: +3V3 -> +1V2
- C231 pad 2: U2_RESET_N -> GND
- C240 pad 1: U2_DN2_TXDP -> U2_UP_TXDP
- C240 pad 2: BAY4_USB3_RX_P -> USB3_1_RX_P
- C241 pad 1: U2_DN1_TXDM -> U2_UP_TXDM
- C241 pad 2: BAY3_USB3_RX_N -> USB3_1_RX_N
- C251 pad 1: U2_DN2_TXDM -> U2_DN1_TXDP
- C251 pad 2: BAY4_USB3_RX_N -> BAY3_USB3_RX_P
- C252 pad 1: 5V_SYS -> U2_DN2_TXDP
- C252 pad 2: (no net) -> BAY4_USB3_RX_P
- C261 pad 1: U10_LXI -> U2_DN1_TXDM
- C261 pad 2: U10_VDD_CORE -> BAY3_USB3_RX_N
- C262 pad 1: U10_XI -> U2_DN2_TXDM
- C262 pad 2: GND -> BAY4_USB3_RX_N
- C3 pad 1: +3V3 -> SD_VDD
- C3 pad 2: SD_PWR_ON -> GND
- C30 pad 1: 3V3_M2_SW -> +3V3
- C31 pad 1: U21_FB -> +1V2
- C310 pad 1: 5V_SYS -> +12V
- C310 pad 2: (no net) -> Q31_G
- C320 pad 1: 5V_HDD -> +12V
- C320 pad 2: Q42_G -> Q32_G
- C340 pad 1: BAY_EN4 -> +12V
- C340 pad 2: BAY4_EN_G -> Q34_G
- C4 pad 1: U1_RBIAS -> +3V3
- C410 pad 1: U11_LXI -> 5V_HDD
- C410 pad 2: U11_VDD_CORE -> Q41_G
- C420 pad 1: 5V_SYS -> 5V_HDD
- C420 pad 2: (no net) -> Q42_G
- C440 pad 1: +12V -> 5V_HDD
- C440 pad 2: Q34_G -> Q44_G
- C500 pad 1: 3V3_M2_SW -> 3V3_M2
- C500 pad 2: M2_PEDET -> GND
- C501 pad 2: PCIE_CLKREQ -> GND
- C502 pad 1: +3V3 -> U50_CT
- C502 pad 2: +3V3 -> GND
- C5100 pad 1: 3V3_M2 -> +12V
- C5101 pad 1: 5V_SYS -> U51_BST
- C5101 pad 2: BZ1_N -> U51_SW
- C5102 pad 1: 3V3_M2_SW -> 3V3_M2
- C5102 pad 2: M2_LED_A -> GND
- C5103 pad 1: U50_CT -> 3V3_M2
- D11 pad 1: U13_LED -> U11_LED
- D11 pad 2: BAY4_LED_A -> BAY2_LED_A
- D12 pad 1: M2_DOOR -> U12_LED
- D12 pad 2: GND -> BAY3_LED_A
- D13 pad 1: VIN_12V_RAW -> U13_LED
- D13 pad 2: VIN_12V_FUSED -> BAY4_LED_A
- D20 pad 1: U21_SW -> GND
- D20 pad 2: 5V_HDD -> VIN_12V_FUSED
- D21 pad 1: U21_EN -> +12V
- D21 pad 2: U21_FB -> Q20_GATE
- D4 pad 1: +3V3 -> 5V_SYS
- D4 pad 2: D2_A -> BZ1_N
- D50 pad 1: +12V -> M2_DAS
- D50 pad 2: Q20_GATE -> M2_LED_A
- F1 pad 1: U22_SW -> VIN_12V_RAW
- F1 pad 2: +3V3 -> VIN_12V_FUSED
- F10 pad 1: Q31_G -> 12V_BAY1_SW
- F10 pad 2: +12V -> 12V_BAY1
- F11 pad 1: 5V_BAY2_SW -> 12V_BAY2_SW
- F11 pad 2: 5V_BAY2 -> 12V_BAY2
- F13 pad 1: BAY4_SATA_B_N -> 12V_BAY4_SW
- F13 pad 2: U13_SRXN -> 12V_BAY4
- F14 pad 1: Q41_G -> 5V_BAY1_SW
- F14 pad 2: 5V_HDD -> 5V_BAY1
- F15 pad 1: Q32_G -> 5V_BAY2_SW
- F15 pad 2: +12V -> 5V_BAY2
- F17 pad 1: 12V_BAY4_SW -> 5V_BAY4_SW
- F17 pad 2: 12V_BAY4 -> 5V_BAY4
- J11 pad P13: 12V_BAY4 -> 12V_BAY2
- J11 pad P14: 12V_BAY4 -> 12V_BAY2
- J11 pad P15: 12V_BAY4 -> 12V_BAY2
- J11 pad P7: 5V_BAY4 -> 5V_BAY2
- J11 pad P8: 5V_BAY4 -> 5V_BAY2
- J11 pad P9: 5V_BAY4 -> 5V_BAY2
- J11 pad S2: BAY4_SATA_A_P -> BAY2_SATA_A_P
- J11 pad S3: BAY4_SATA_A_N -> BAY2_SATA_A_N
- J11 pad S5: BAY4_SATA_B_N -> BAY2_SATA_B_N
- J11 pad S6: BAY4_SATA_B_P -> BAY2_SATA_B_P
- J50 pad 1: +12V -> (no net)
- J50 pad 2: GND -> 3V3_M2_SW
- L10 pad 1: U10_VDD_CORE -> U10_LXI
- L10 pad 2: GND -> U10_VDD_CORE
- L11 pad 1: U11_XI -> U11_LXI
- L11 pad 2: GND -> U11_VDD_CORE
- L13 pad 1: 5V_SYS -> U13_LXI
- L13 pad 2: (no net) -> U13_VDD_CORE
- L20 pad 1: +3V3 -> U20_SW
- L20 pad 2: GND -> 5V_SYS
- L21 pad 1: +12V -> U21_SW
- L21 pad 2: GND -> 5V_HDD
- L22 pad 1: +12V -> U22_SW
- L22 pad 2: GND -> +3V3
- L51 pad 1: +12V -> U51_SW
- L51 pad 2: GND -> 3V3_M2
- Q1 pad 1: SD_VDD -> Q1_GATE
- Q20 pad 1: U20_SW -> Q20_GATE
- Q20 pad 2: 5V_SYS -> +12V
- Q31 pad 1: BAY1_EN_G -> Q31_G
- Q31 pad 2: GND -> +12V
- Q31 pad 3: Q51_D -> 12V_BAY1_SW
- Q32 pad 1: Q42_G -> Q32_G
- Q32 pad 2: 5V_HDD -> +12V
- Q32 pad 3: 5V_BAY2_SW -> 12V_BAY2_SW
- Q34 pad 1: 5V_BAY4_SW -> Q34_G
- Q34 pad 2: 5V_BAY4 -> +12V
- Q41 pad 1: BAY1_EN_G -> Q41_G
- Q41 pad 2: GND -> 5V_HDD
- Q41 pad 3: Q61_D -> 5V_BAY1_SW
- Q42 pad 1: BAY2_EN_G -> Q42_G
- Q42 pad 2: GND -> 5V_HDD
- Q42 pad 3: Q52_D -> 5V_BAY2_SW
- Q44 pad 1: Q34_G -> Q44_G
- Q44 pad 2: +12V -> 5V_HDD
- Q44 pad 3: 12V_BAY4_SW -> 5V_BAY4_SW
- Q51 pad 1: +12V -> BAY1_EN_G
- Q51 pad 2: Q31_G -> GND
- Q52 pad 3: Q62_D -> Q52_D
- Q54 pad 1: Q44_G -> BAY4_EN_G
- Q54 pad 2: 5V_HDD -> GND
- Q54 pad 3: 5V_BAY4_SW -> Q54_D
- Q61 pad 1: Q31_G -> BAY1_EN_G
- Q61 pad 2: Q51_D -> GND
- Q62 pad 1: +12V -> BAY2_EN_G
- Q62 pad 2: Q32_G -> GND
- Q64 pad 3: Q54_D -> Q64_D
- R1 pad 1: BUZZER -> +3V3
- R1 pad 2: Q1_GATE -> D1_A
- R10 pad 2: ETH_LED_Y_A -> FAN_PWM
- R100 pad 1: +3V3 -> U1_RBIAS
- R100 pad 2: U1_PRT_DIS_P3 -> GND
- R1000 pad 1: U10_VCCO -> U10_REXT
- R1000 pad 2: BAY1_LED_A -> GND
- R1001 pad 1: U10_XI -> U10_VCCO
- R1001 pad 2: GND -> U10_RST
- R1002 pad 1: U10_XO -> U10_VCCO
- R1002 pad 2: GND -> BAY1_LED_A
- R101 pad 2: U1_PRT_DIS_P4 -> U1_VBUS_DET
- R102 pad 2: U1_PRT_DIS_M3 -> U1_RESET_N
- R103 pad 1: +3V3 -> U1_CFG_NON_REM
- R103 pad 2: U1_PRT_DIS_M4 -> GND
- R11 pad 2: GND -> SD_PWR_ON
- R1100 pad 1: U11_VCCO -> U11_REXT
- R1100 pad 2: U11_RST -> GND
- R1101 pad 2: BAY2_LED_A -> U11_RST
- R1102 pad 1: U11_XI -> U11_VCCO
- R1102 pad 2: GND -> BAY2_LED_A
- R113 pad 1: U1_XTALI -> +3V3
- R113 pad 2: GND -> U1_PRT_DIS_P3
- R114 pad 1: U1_XTALO -> +3V3
- R114 pad 2: GND -> U1_PRT_DIS_P4
- R123 pad 2: GND -> U1_PRT_DIS_M3
- R124 pad 2: GND -> U1_PRT_DIS_M4
- R1300 pad 1: U13_RST -> U13_REXT
- R1301 pad 1: U13_REXT -> U13_VCCO
- R1301 pad 2: GND -> U13_RST
- R1302 pad 2: U13_RST -> BAY4_LED_A
- R2 pad 1: Q1_GATE -> +3V3
- R2 pad 2: GND -> D2_A
- R20 pad 1: +3V3 -> Q20_GATE
- R20 pad 2: +12V -> GND
- R200 pad 1: U2_CFG_NON_REM -> U2_RBIAS
- R2000 pad 1: +12V -> 5V_SYS
- R2000 pad 2: U21_EN -> U20_FB
- R2001 pad 1: 5V_HDD -> U20_FB
- R2001 pad 2: PG_5V_HDD -> GND
- R2002 pad 1: U20_BOOT -> +12V
- R2002 pad 2: U20_SW -> U20_EN
- R2003 pad 1: U21_BOOT -> 5V_SYS
- R2003 pad 2: U21_SW -> PG_5V_SYS
- R201 pad 2: U2_PRT_DIS_P3 -> U2_VBUS_DET
- R202 pad 2: U2_PRT_DIS_P4 -> U2_RESET_N
- R203 pad 1: +3V3 -> U2_CFG_NON_REM
- R203 pad 2: U2_PRT_DIS_M3 -> GND
- R2100 pad 1: U22_BST -> 5V_HDD
- R2100 pad 2: U22_SW -> U21_FB
- R2101 pad 1: +3V3 -> U21_FB
- R2102 pad 1: U51_SW -> +12V
- R2102 pad 2: 3V3_M2 -> U21_EN
- R2103 pad 1: 3V3_M2 -> 5V_HDD
- R2103 pad 2: +12V -> PG_5V_HDD
- R213 pad 2: U2_PRT_DIS_M4 -> U2_PRT_DIS_P3
- R214 pad 1: U2_XTALI -> +3V3
- R214 pad 2: GND -> U2_PRT_DIS_P4
- R223 pad 1: U2_XTALO -> +3V3
- R223 pad 2: GND -> U2_PRT_DIS_M3
- R224 pad 2: GND -> U2_PRT_DIS_M4
- R3 pad 2: ETH_LED_G_A -> D3_A
- R310 pad 1: 5V_HDD -> +12V
- R310 pad 2: Q41_G -> Q31_G
- R311 pad 1: Q41_G -> Q31_G
- R311 pad 2: Q61_D -> Q51_D
- R320 pad 1: Q32_G -> +12V
- R320 pad 2: Q52_D -> Q32_G
- R321 pad 1: 5V_HDD -> Q32_G
- R321 pad 2: Q42_G -> Q52_D
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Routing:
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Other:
- board size 180 x 110 mm -> 150 x 98 mm
- board text added: "brain-drain carrier v1 150x98 rear edge = top"
- board text removed: "brain-drain carrier v0 180x110 rear edge = top"
